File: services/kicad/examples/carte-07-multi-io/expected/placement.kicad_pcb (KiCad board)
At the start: 2 copper layers, 110 x 80 mm, 44 parts, among them J1 IN_5V, J10 IO0, J11 IO1, J12 IO2, J2 SWD, U1 STM32F103C8T6, U2 AMS1117-3.3

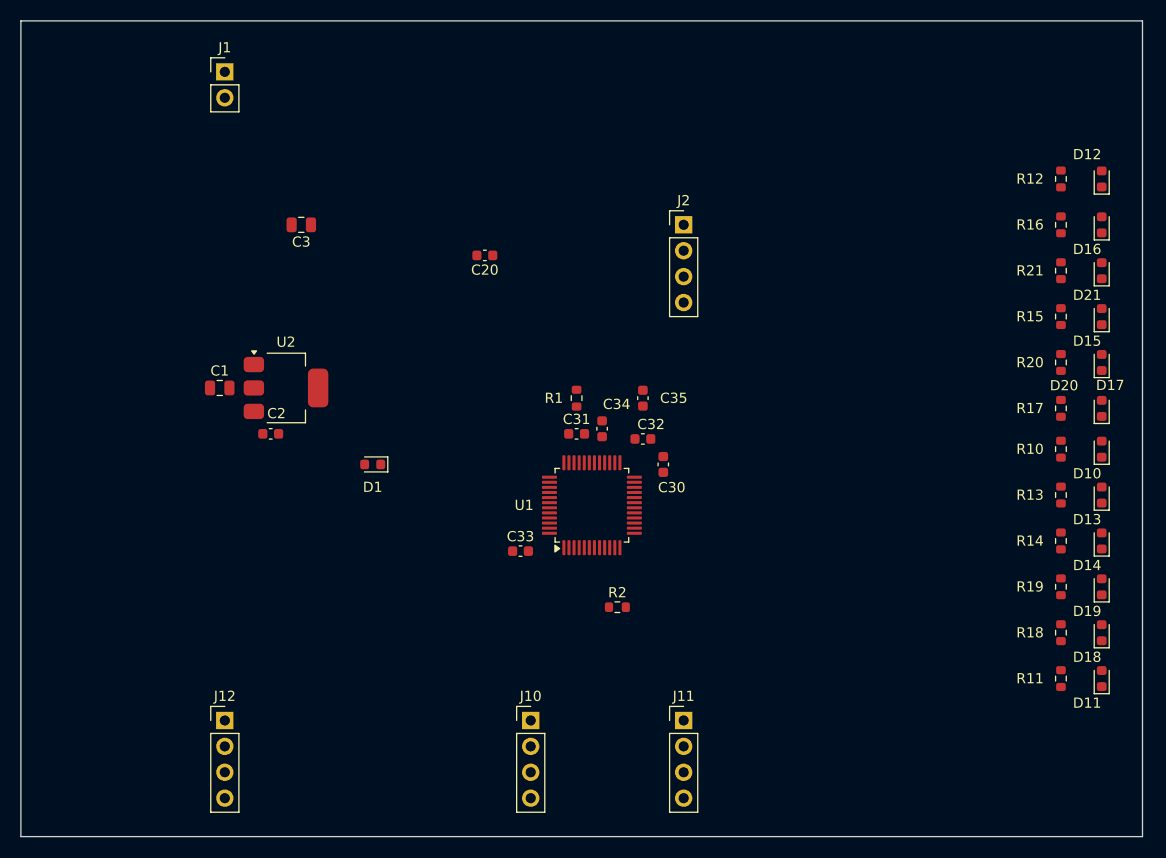
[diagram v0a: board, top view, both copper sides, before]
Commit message: test(examples): quatre cartes livrées plus petites — contour resserré mesuré sur le banc (D-2026-09-13-c A)
Banc rejoué en taille heuristique (phase 1 puis phase 2 à placement gelé) :
carte-01 25x20 -> 24,8x17 (84 % de surface), carte-04 60x45 -> 45x44,8
(75 %), carte-06 80x60 -> 65,2x59,8 (81 %), carte-07 110x80 -> 99,5x79,8
(90 %) — toutes 100 % routées, 0 erreur DRC (vérifié en local), rendus 3D
régénérés. Gain nul sur les cartes denses (le génétique remplit la carte) ;
08 et 09 non livrées (dispersion du routage, surface inchangée) ; carte-11
non livrée (carte d'escalade). Tableau complet dans docs/DECISIONS.md.

Co-Authored-By: Claude Fable 5.1 <noreply@anthropic.com>
Claude-Session: https://claude.ai/code/session_01TnMqm4La2CxQHHB5K8aSSV
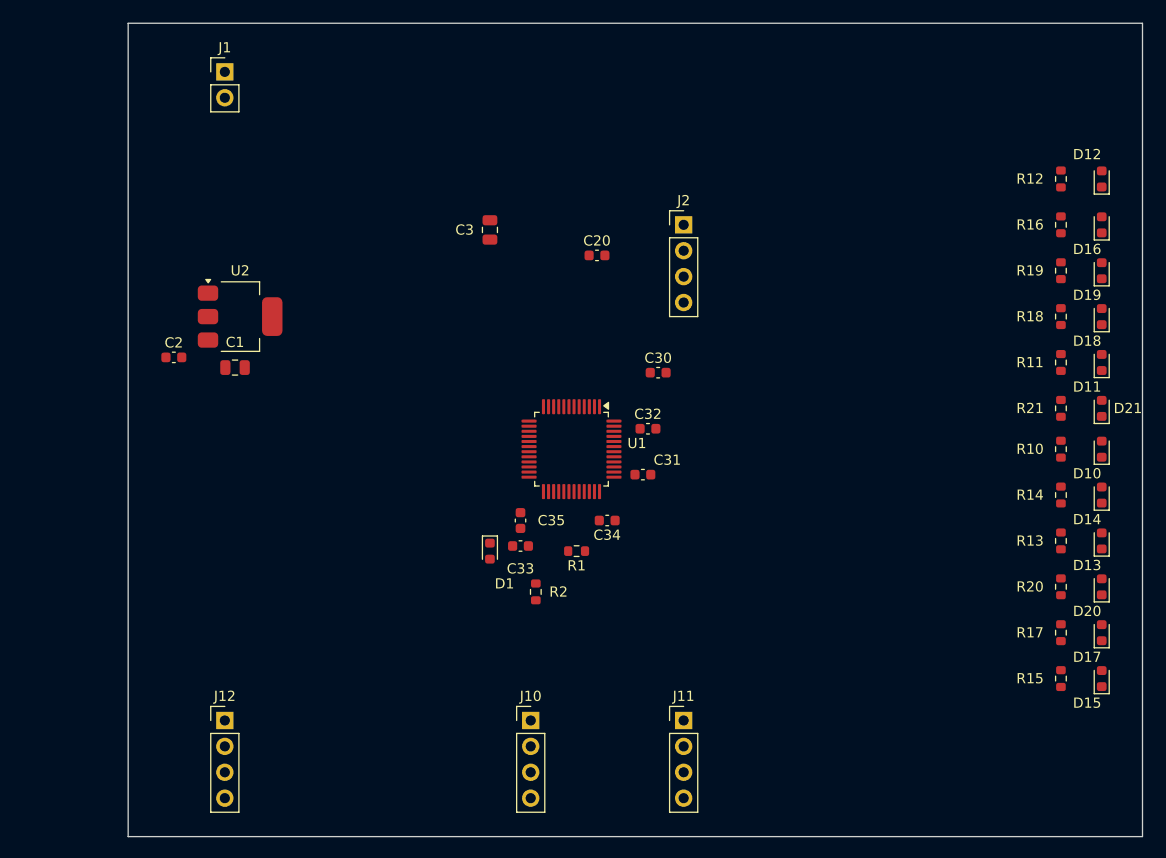
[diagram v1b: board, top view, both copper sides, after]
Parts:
- moved D15 35.5 mm to (199.5, 129.5)
- moved R15 35.5 mm to (195.5, 129.5)
- moved D11 31.0 mm to (199.5, 98.5)
- moved D18 31.0 mm to (199.5, 94.0)
- moved D19 31.0 mm to (199.5, 89.5)
- moved R11 31.0 mm to (195.5, 98.5)
- moved R18 31.0 mm to (195.5, 94.0)
- moved R19 31.0 mm to (195.5, 89.5)
- moved D17 22.0 mm to (199.5, 125.0)
- moved D20 22.0 mm to (199.5, 120.5)
- moved R17 22.0 mm to (195.5, 125.0)
- moved R20 22.0 mm to (195.5, 120.5)
- moved C3 18.5 mm to (139.5, 85.5), turned to 90 degrees
- moved C35 17.0 mm to (142.5, 114.0)
- moved R1 15.0 mm to (148.0, 117.0), turned to 180 degrees
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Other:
- board size 110 x 80 mm -> 99.5 x 79.8 mm

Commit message: fix(kicad): plan de masse referme — banc DIX cartes sur dix, 0 erreur 0 manquante (#237)
* docs(kicad): la derniere rupture de plan tient a UN segment, pas a un faisceau

Diagnostic complet du seul defaut restant du banc (carte-10), mesure sur le
board qui le porte vraiment, apres consultation de Codex et de GLM.

Mesures sur `/tmp/livr/carte-10-maximale/route.kicad_pcb` (33 violations,
0 erreur, 1 connexion manquante) :

- 23 ilots GND sur les deux faces, exactement 2 orphelins, et ce sont des
  JUMEAUX : F.Cu 1,30 mm2 (porte la pastille C35.2) et B.Cu 0,99 mm2.
- AUCUN de leurs points n a le plan principal en vis-a-vis : ils se font face
  l un l autre. La piste « changer de face par un via », proposee par GLM, est
  donc REFUTEE par la mesure.
- La couture de production visite les deux ilots et refuse la totalite de
  leurs sites (23 et 18 candidats ; obstacle 16/10, hors_polygone 6/7,
  trou_trop_pres 1/1) : un via ne tient pas dans un millimetre carre.
  Le raccord par courte piste rend relies 0, sans_chemin 19.
- Mais le plan principal n est qu a 0,862 mm sur F.Cu et 0,781 mm sur B.Cu, et
  UN SEUL segment coupe le couloir de chaque face (EXT2_1, EXT4_1).

Le plan de Codex — deplacer l obstacle au lieu de chercher un passage a
travers — a donc ici un ensemble a arracher d UN segment par face, pas une
recherche ouverte. Decision de strategie de routage : D-2026-09-22-a, EN
ATTENTE. Rien n est implemente.

Levier natif verifie et jamais appele : LocalRerouter.reroute_segment() de
kicad-tools, utilise par drc/repair_clearance.py, zero appelant Cirqix. Il
travaille sur le document S-expression quand notre code travaille sur pcbnew.

Lecons inscrites dans CLAUDE.md :
- j ai d abord mesure le board VERSIONNE du 21, qui est propre (non_connectes
  0) et se pretait a toutes les demonstrations — un via y tenait avec 0,29 mm
  de marge. Verifier que l artefact PORTE le defaut avant de le diagnostiquer.
- ma premiere sonde raisonnait zone par zone, alors que la carte por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
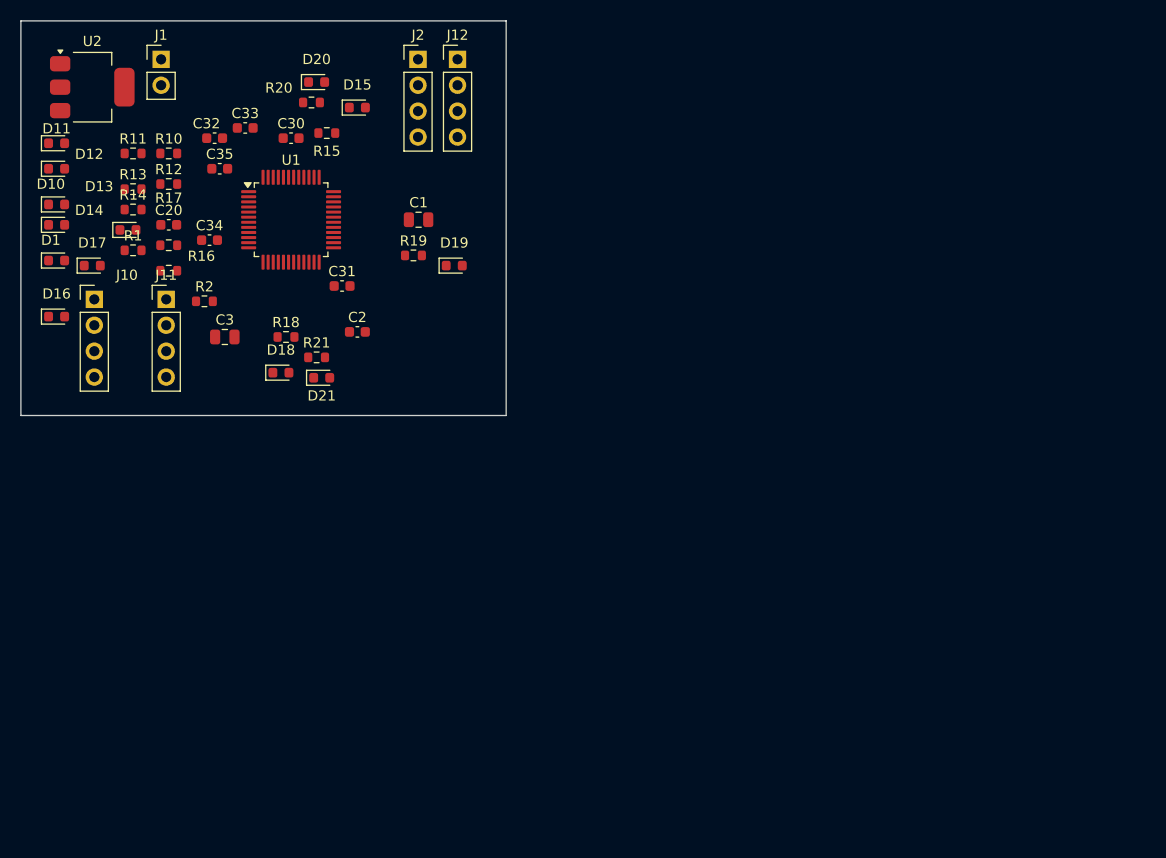
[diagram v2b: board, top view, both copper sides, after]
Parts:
- moved D14 105.9 mm to (97.0, 85.0), turned to 0 degrees
- moved D17 105.3 mm to (100.5, 89.0), turned to 0 degrees
- moved D10 105.3 mm to (97.0, 83.0), turned to 0 degrees
- moved D11 104.7 mm to (97.0, 77.0), turned to 0 degrees
- moved D16 102.9 mm to (97.0, 94.0), turned to 0 degrees
- moved D12 102.5 mm to (97.0, 79.5), turned to 0 degrees
- moved D13 100.3 mm to (104.0, 85.5), turned to 0 degrees
- moved R13 97.3 mm to (104.5, 81.5), turned to 0 degrees
- moved R17 95.4 mm to (108.0, 87.0), turned to 0 degrees
- moved R14 95.2 mm to (104.5, 83.5), turned to 0 degrees
- moved R11 93.3 mm to (104.5, 78.0), turned to 0 degrees
- moved R10 92.2 mm to (108.0, 78.0), turned to 0 degrees
- moved D15 92.0 mm to (126.5, 73.5), turned to 0 degrees
- moved D20 91.5 mm to (122.5, 71.0), turned to 0 degrees
- moved R15 89.7 mm to (123.5, 76.0), turned to 0 degrees
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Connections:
- U1 pad 36: Net-(U1-36) -> PWR_FLAG
- U1 pad 48: Net-(U1-48) -> PWR_FLAG
- U1 pad 9: IO_L5 -> PWR_FLAG
- U2 pad 3: VIN -> PWR_FLAG
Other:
- board size 99.5 x 79.8 mm -> 47.6 x 38.7 mm

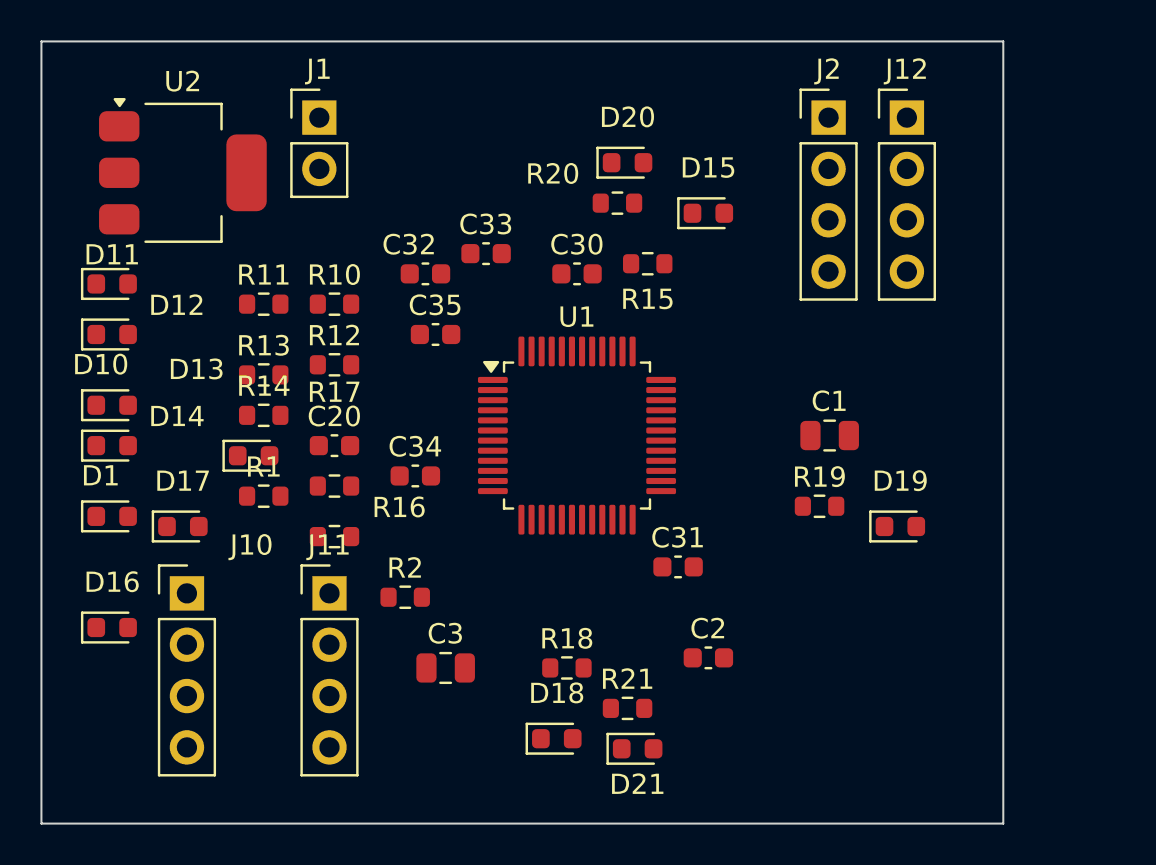
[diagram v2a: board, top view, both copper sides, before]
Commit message: feat(routing): routage prioritaire des liaisons critiques, et une pastille un proprietaire
D-2026-09-25-a (validee : « propose toi et fais tout selon votre
recommandation »). Avant Freerouting, tools/nets_critiques.py detecte par la
topologie les liaisons critiques - quartz, charges du quartz, decouplages -
et l'operation runner relier_liaisons les pose par des pistes courtes, sur
une face, sans via, en evitant les vias reserves. Elles sont protegees avec
la liaison GND. Limite : corps a 3 mm au plus (comme le cluster natif) et
piste a 6 mm au plus. Paires differentielles detectees, jamais routees.
Desactive par defaut (reglage routage_prioritaire) jusqu'a la mesure A/B,
un tirage sur deux quand il est actif.

Mesure de detection : 2 a 9 decouplages par carte, aucun quartz retenu -
ils sont a 9-27 mm des broches OSC. Le defaut dominant est le placement.

Etape 0, deux corrections du DSN envoye a Freerouting :
- une pastille, un proprietaire : un via reserve a moins de 0,5 mm d'un via
  protege est ecarte avec son troncon, et un element protege ecrit deux
  fois ne l'est qu'une (4 vias au meme point mesures : 7 s -> 220 s et plus,
  puis HTTP 500 en production) ;
- fuite d'etat : en entrant dans un palier sans protection voulue, la
  liaison GND du palier precedent restait protegee.

D-2026-09-24-g : chaque palier repart libre (le tirage protege echouait a
chaque changement de palier). carte-07 livree : 100 %, 4 couches, 0 erreur,
aucun court-circuit vs schema.

Co-Authored-By: Claude Opus 5.5 <noreply@anthropic.com>
Claude-Session: https://claude.ai/code/session_01TnMqm4La2CxQHHB5K8aSSV
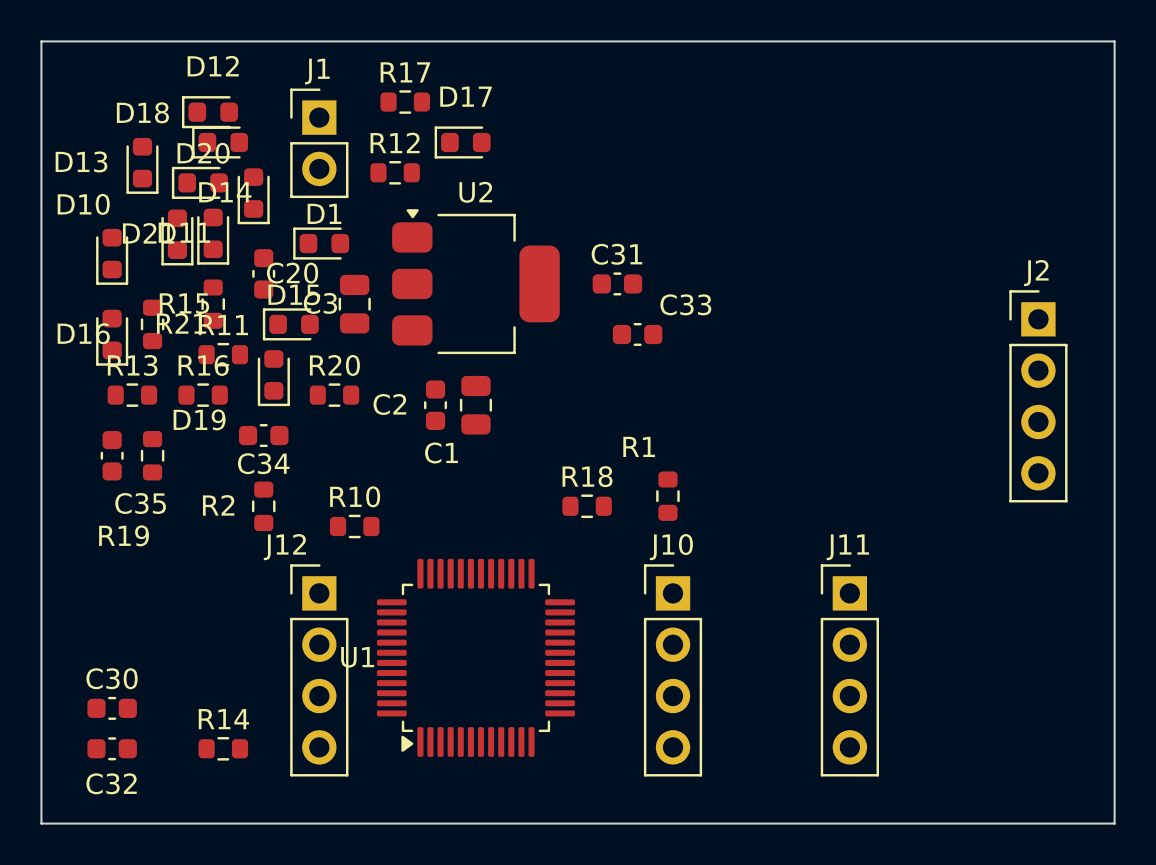
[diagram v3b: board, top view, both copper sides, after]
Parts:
- moved J12 37.4 mm to (107.2, 92.3)
- moved D21 34.2 mm to (100.2, 74.5), turned to 90 degrees
- moved D18 33.8 mm to (102.5, 70.0)
- moved R19 33.1 mm to (99.0, 85.5), turned to 90 degrees
- moved D19 31.9 mm to (105.0, 81.5), turned to 90 degrees
- moved C30 31.5 mm to (97.0, 98.0)
- moved R21 30.2 mm to (99.0, 79.0), turned to 270 degrees
- moved C32 28.2 mm to (97.0, 100.0)
- moved J11 25.7 mm to (133.5, 92.3)
- moved J10 24.0 mm to (124.8, 92.3)
- moved D17 23.6 mm to (114.5, 70.0)
- moved R15 21.6 mm to (102.0, 78.0), turned to 90 degrees
- moved D15 21.2 mm to (106.0, 79.0)
- moved D20 21.0 mm to (101.5, 72.0)
- moved R1 20.0 mm to (124.5, 87.5), turned to 90 degrees
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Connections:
- C3 pad 1: Net-(C3-1) -> +3V3
- U1 pad 36: PWR_FLAG -> +3V3
- U1 pad 48: PWR_FLAG -> +3V3
- U1 pad 9: PWR_FLAG -> IO_L5
- U2 pad 2: Net-(U2-2) -> +3V3
- U2 pad 3: PWR_FLAG -> VIN
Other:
- board size 47.6 x 38.7 mm -> 53.1 x 38.7 mm
